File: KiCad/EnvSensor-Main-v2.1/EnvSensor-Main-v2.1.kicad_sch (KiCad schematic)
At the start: 90 parts, among them J6 POWER_INPUT, Q1 IRLML2502

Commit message: Finishing touhches on main board
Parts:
- D?: value SD_LED -> LED
- D?: value CPU_LED -> LED
- J?: footprint Connector_PinHeader_2.54mm:PinHeader_1x06_P2.54mm_Vertical -> Connector_JST:JST_PH_S6B-PH-SM4-TB_1x06-1MP_P2.00mm_Horizontal
- J?: footprint Connector_PinHeader_2.54mm:PinHeader_1x04_P2.54mm_Vertical -> Connector_JST:JST_PH_S4B-PH-SM4-TB_1x04-1MP_P2.00mm_Horizontal
- L?: footprint Inductor_SMD:L_0805_2012Metric -> Inductor_SMD:L_1206_3216Metric
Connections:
- net +5V: now also C23.1, C24.1, C25.1
- net BMP280_VCC: now also JP3.3 (B); no longer JP3.1 (A)
- net GND: now also C23.2, C24.2, C25.2, JP3.1 (A); no longer JP3.3 (B)
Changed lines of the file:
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@@
   (junction (at 346.71 190.5) (diameter 0) (color 0 0 0 0)
   )
+  (junction (at 386.08 39.37) (diameter 0) (color 0 0 0 0)
+  )
   (junction (at 232.41 194.31) (diameter 0) (color 0 0 0 0)
   )
   (junction (at 209.55 77.47) (diameter 0) (color 0 0 0 0)
   )
+  (junction (at 381 39.37) (diameter 0) (color 0 0 0 0)
+  )
   (junction (at 232.41 162.56) (diameter 0) (color 0 0 0 0)
   )
@@
   (junction (at 88.9 254) (diameter 0) (color 0 0 0 0)
   )
+  (junction (at 391.16 49.53) (diameter 0) (color 0 0 0 0)
+  )
+  (junction (at 386.08 49.53) (diameter 0) (color 0 0 0 0)
+  )
   (junction (at 101.6 29.21) (diameter 0) (color 0 0 0 0)
   )
@@
     (stroke (width 0) (type default))
   )
+  (wire (pts (xy 391.16 49.53) (xy 396.24 49.53))
+    (stroke (width 0) (type default))
+  )
   (wire (pts (xy 240.03 162.56) (xy 243.84 162.56))
     (stroke (width 0) (type default))
@@
     (stroke (width 0) (type default))
   )
+  (wire (pts (xy 377.19 39.37) (xy 381 39.37))
+    (stroke (width 0) (type default))
+  )
   (wire (pts (xy 34.29 113.03) (xy 26.67 113.03))
     (stroke (width 0) (type default))
@@
     (stroke (width 0) (type default))
   )
+  (wire (pts (xy 381 38.1) (xy 381 39.37))
+    (stroke (width 0) (type default))
+  )
   (polyline (pts (xy 148.59 283.21) (xy 148.59 223.52))
     (stroke (width 0) (type default))
@@
     (stroke (width 0) (type default))
   )
+  (wire (pts (xy 377.19 48.26) (xy 377.19 49.53))
+    (stroke (width 0) (type default))
+  )
   (polyline (pts (xy 231.14 96.52) (xy 231.14 22.86))
     (stroke (width 0) (type default))
@@
     (stroke (width 0) (type default))
   )
+  (wire (pts (xy 396.24 49.53) (xy 396.24 48.26))
+    (stroke (width 0) (type default))
+  )
   (wire (pts (xy 224.79 194.31) (xy 232.41 194.31))
     (stroke (width 0) (type default))
@@
     (stroke (width 0) (type default))
   )
+  (wire (pts (xy 377.19 49.53) (xy 386.08 49.53))
+    (stroke (width 0) (type default))
+  )
   (wire (pts (xy 48.26 252.73) (xy 48.26 254))
     (stroke (width 0) (type default))
@@
     (stroke (width 0) (type default))
   )
+  (wire (pts (xy 381 39.37) (xy 386.08 39.37))
+    (stroke (width 0) (type default))
+  )
   (wire (pts (xy 224.79 189.23) (xy 247.65 189.23))
     (stroke (width 0) (type default))
@@
     (stroke (width 0) (type default))
   )
+  (wire (pts (xy 386.08 39.37) (xy 386.08 40.64))
+    (stroke (width 0) (type default))
+  )
   (wire (pts (xy 92.71 29.21) (xy 92.71 31.75))
     (stroke (width 0) (type default))
@@
     (stroke (width 0) (type default))
   )
+  (wire (pts (xy 386.08 39.37) (xy 396.24 39.37))
+    (stroke (width 0) (type default))
+  )
   (wire (pts (xy 90.17 92.71) (xy 97.79 92.71))
     (stroke (width 0) (type default))
@@
     (stroke (width 0) (type default))
   )
+  (wire (pts (xy 396.24 39.37) (xy 396.24 40.64))
+    (stroke (width 0) (type default))
+  )
   (wire (pts (xy 248.92 256.54) (xy 246.38 256.54))
     (stroke (width 0) (type default))
@@
     (stroke (width 0) (type default))
   )
+  (wire (pts (xy 377.19 40.64) (xy 377.19 39.37))
+    (stroke (width 0) (type default))
+  )
   (wire (pts (xy 182.88 195.58) (xy 182.88 198.12))
     (stroke (width 0) (type default))
@@
     (stroke (width 0) (type default))
   )
+  (wire (pts (xy 386.08 49.53) (xy 391.16 49.53))
+    (stroke (width 0) (type default))
+  )
   (wire (pts (xy 86.36 255.27) (xy 86.36 254))
     (stroke (width 0) (type default))
@@
     (stroke (width 0) (type default))
   )
+  (wire (pts (xy 386.08 48.26) (xy 386.08 49.53))
+    (stroke (width 0) (type default))
+  )
   (wire (pts (xy 152.4 71.12) (xy 152.4 77.47))
     (stroke (width 0) (type default))
@@
     (stroke (width 0) (type default))
   )
+  (wire (pts (xy 391.16 49.53) (xy 391.16 52.07))
+    (stroke (width 0) (type default))
+  )
   (wire (pts (xy 44.45 176.53) (xy 53.34 176.53))
     (stroke (width 0) (type default))
@@
     )
   )
+  (symbol (lib_id "power:+5V") (at 381 38.1 0) (unit 1)
+    (in_bom yes) (on_board yes) (dnp no)
+    (property "Reference" "#PWR?" (at 381 41.91 0)
+      (effects (font (size 1.27 1.27)) hide)
+    )
+    (property "Value" "+5V" (at 381.381 33.7058 0)
+      (effects (font (size 1.27 1.27)))
+    )
+    (property "Footprint" "" (at 381 38.1 0)
+      (effects (font (size 1.27 1.27)) hide)
+    )
+    (property "Datasheet" "" (at 381 38.1 0)
+      (effects (font (size 1.27 1.27)) hide)
+    )
+    (pin "1")
+    (instances
+      (project "EnvSensor-v2"
+        (path "/03d24414-d9e0-4f5b-b242-97cf8b84dd63"
+          (reference "#PWR?") (unit 1)
+        )
+      )
+      (project "EnvSensor-Main-v2.1"
+        (path "/dfd093c6-2284-47ad-b656-d7ad8b97da97"
+          (reference "#PWR057") (unit 1)
+        )
+      )
+    )
+  )
   (symbol (lib_id "Device:R") (at 252.73 256.54 270) (unit 1)
     (in_bom yes) (on_board yes) (dnp no)
@@
       (effects (font (size 1.27 1.27)) (justify right))
     )
-    (property "Value" "SD_LED" (at 52.07 255.27 90)
+    (property "Value" "LED" (at 52.07 255.27 90)
       (effects (font (size 1.27 1.27)) (justify right))
     )
@@
       (effects (font (size 1.27 1.27)) (justify left))
     )
-    (property "Footprint" "Connector_PinHeader_2.54mm:PinHeader_1x06_P2.54mm_Vertical" (at 53.34 213.36 0)
+    (property "Footprint" "Connector_JST:JST_PH_S6B-PH-SM4-TB_1x06-1MP_P2.00mm_Horizontal" (at 53.34 213.36 0)
       (effects (font (size 1.27 1.27)) hide)
     )
@@
       (effects (font (size 1.27 1.27)) (justify left))
     )
-    (property "Footprint" "Connector_PinHeader_2.54mm:PinHeader_1x04_P2.54mm_Vertical" (at 377.19 57.15 0)
+    (property "Footprint" "Connector_JST:JST_PH_S4B-PH-SM4-TB_1x04-1MP_P2.00mm_Horizontal" (at 377.19 57.15 0)
       (effects (font (size 1.27 1.27)) hide)
     )
@@
       (effects (font (size 1.27 1.27)))
     )
-    (property "Footprint" "Inductor_SMD:L_0805_2012Metric" (at 83.82 29.21 0)
+    (property "Footprint" "Inductor_SMD:L_1206_3216Metric" (at 83.82 29.21 0)
       (effects (font (size 1.27 1.27)) hide)
     )
@@
     )
   )
+  (symbol (lib_id "power:GND") (at 391.16 52.07 0) (unit 1)
+    (in_bom yes) (on_board yes) (dnp no)
+    (property "Reference" "#PWR?" (at 391.16 58.42 0)
+      (effects (font (size 1.27 1.27)) hide)
+    )
+    (property "Value" "GND" (at 391.287 56.4642 0)
+      (effects (font (size 1.27 1.27)))
+    )
+    (property "Footprint" "" (at 391.16 52.07 0)
+      (effects (font (size 1.27 1.27)) hide)
+    )
+    (property "Datasheet" "" (at 391.16 52.07 0)
+      (effects (font (size 1.27 1.27)) hide)
+    )
+    (pin "1")
+    (instances
+      (project "EnvSensor-v2"
+        (path "/03d24414-d9e0-4f5b-b242-97cf8b84dd63"
+          (reference "#PWR?") (unit 1)
+        )
+      )
+      (project "EnvSensor-Main-v2.1"
+        (path "/dfd093c6-2284-47ad-b656-d7ad8b97da97"
+          (reference "#PWR056") (unit 1)
+        )
+      )
+    )
+  )
   (symbol (lib_id "EnvSensor-v2-rescue:Jumper_NO_Small-Device") (at 300.99 43.18 90) (unit 1)
     (in_bom yes) (on_board yes) (dnp no)
@@
       (effects (font (size 1.016 1.016)))
     )
-    (property "Value" "ESP-12S" (at 335.28 122.3772 0)
+    (property "Value" "ESP-12S" (at 339.09 125.73 0)
       (effects (font (size 1.016 1.016)))
     )
@@
       (effects (font (size 1.27 1.27)) (justify right))
     )
-    (property "Value" "CPU_LED" (at 31.75 255.27 90)
+    (property "Value" "LED" (at 31.75 255.27 90)
       (effects (font (size 1.27 1.27)) (justify right))
     )
@@
     )
   )
-  (symbol (lib_id "Jumper:Jumper_3_Bridged12") (at 293.37 57.15 270) (unit 1)
+  (symbol (lib_id "Jumper:Jumper_3_Bridged12") (at 293.37 57.15 270) (mirror x) (unit 1)
     (in_bom yes) (on_board yes) (dnp no)
-    (property "Reference" "JP3" (at 294.9962 56.5063 90)
+    (property "Reference" "JP3" (at 294.9962 57.7937 90)
       (effects (font (size 1.27 1.27)) (justify left))
     )
-    (property "Value" "Address" (at 294.64 58.42 90)
+    (property "Value" "Address" (at 294.64 55.88 90)
       (effects (font (size 1.27 1.27)) (justify left))
     )

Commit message: Finishing touches
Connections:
- net SCD_POWER: now reaches J?.1 (Pin_1), JP?.1, U?.1 (VDD), U?.19 (VDDH), U?.7 (VDD)

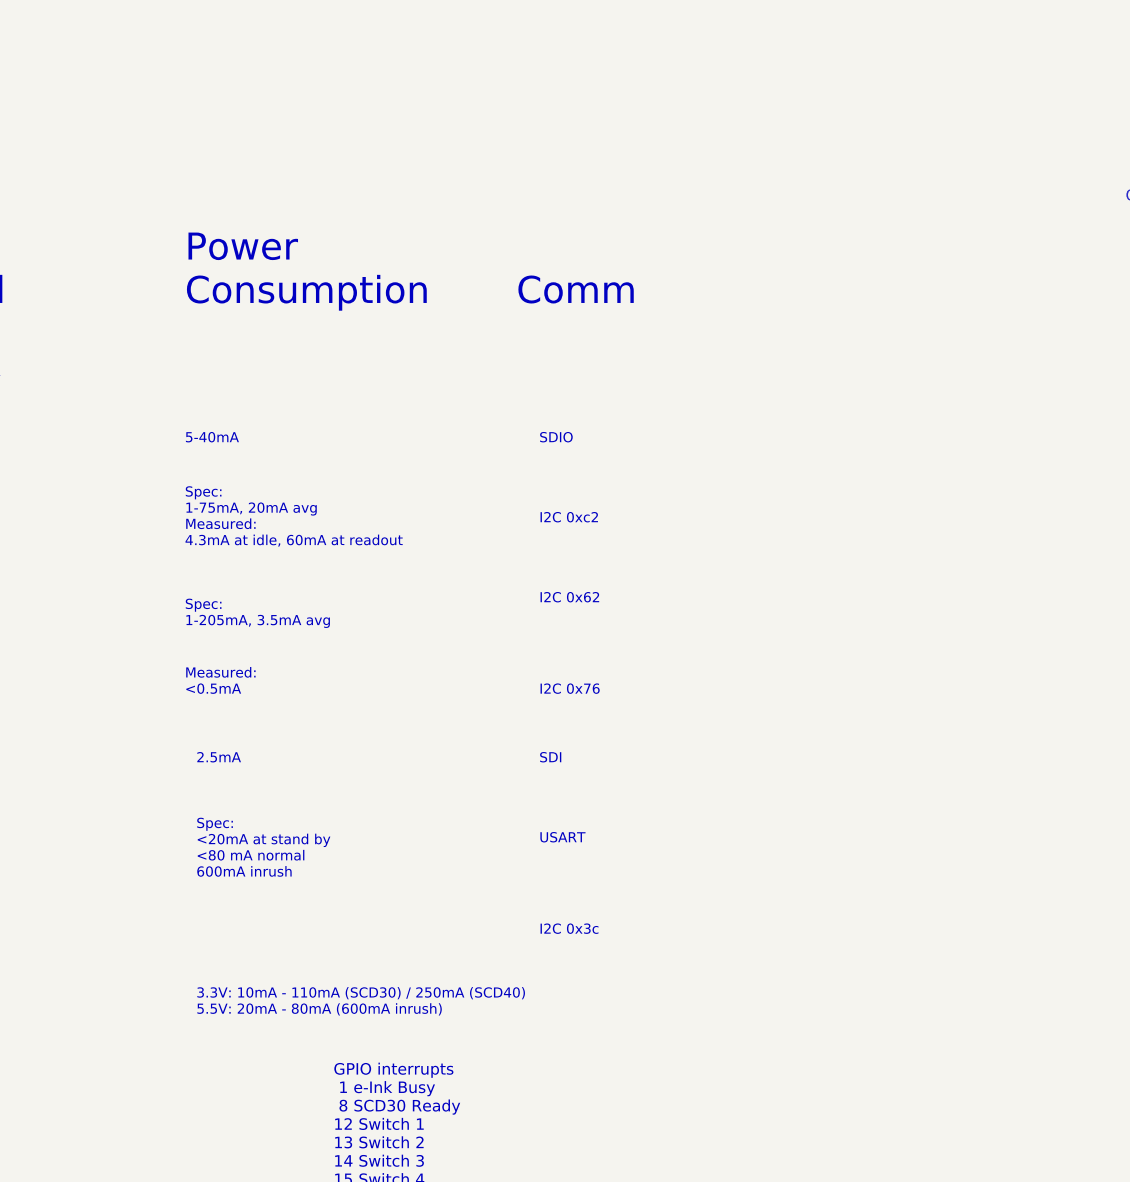
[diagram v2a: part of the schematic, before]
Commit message: LM2735 fixes
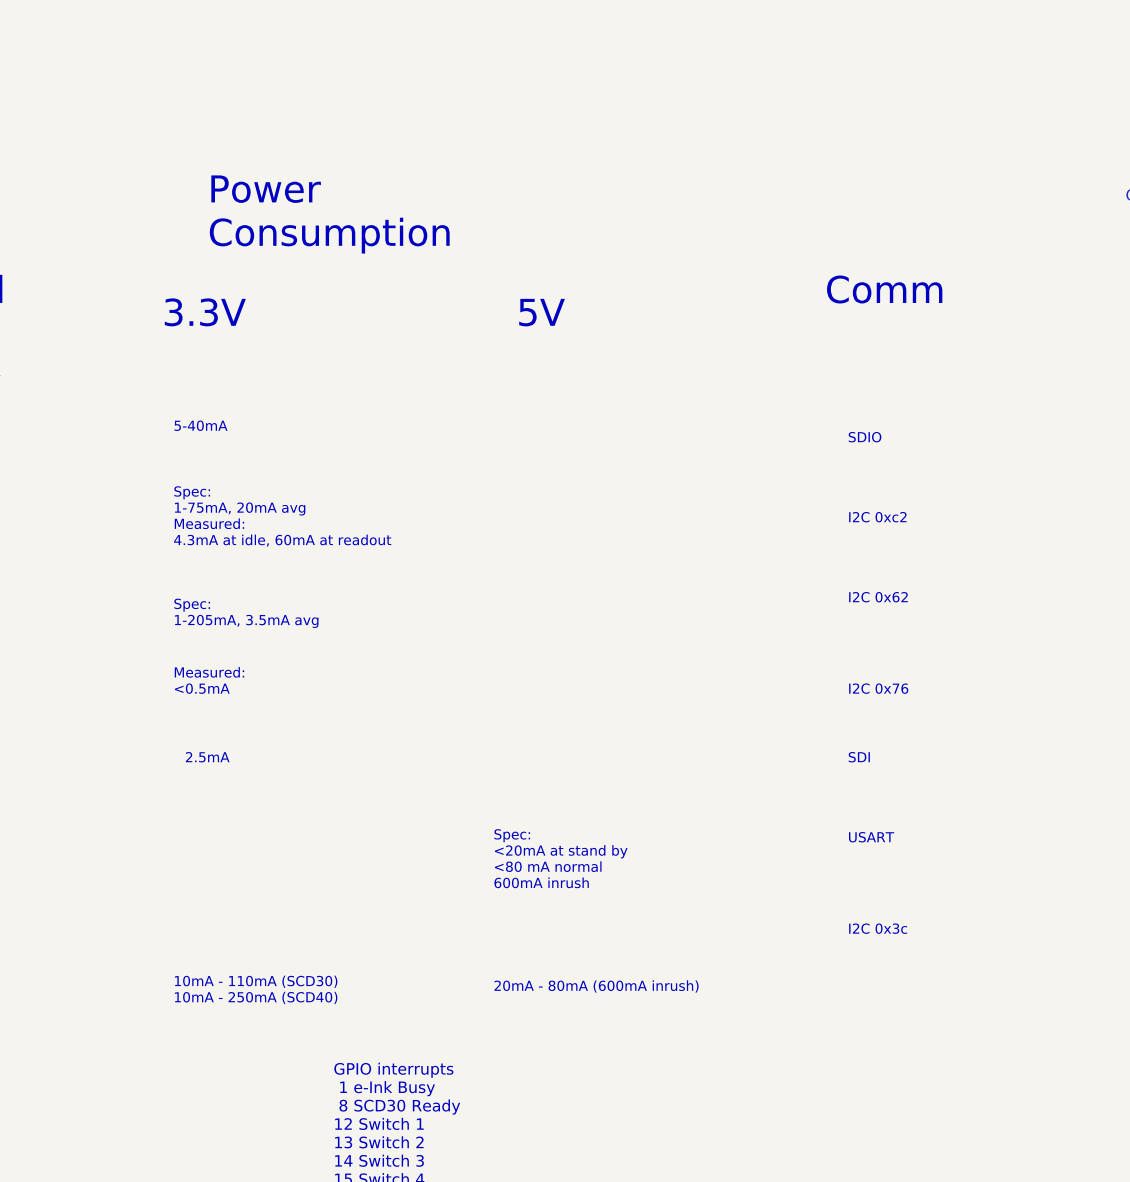
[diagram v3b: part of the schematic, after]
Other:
- note added: "10mA - 110mA (SCD30) 10mA - 250mA (SCD40)"
- note added: "20mA - 80mA (600mA inrush)"
- note added: "5V"
- note removed: "3.3V: 10mA - 110mA (SCD30) / 250mA (SCD40) 5.5V: 20mA - 80mA (600mA inrush)"
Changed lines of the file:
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@@
     (effects (font (size 2.9972 2.9972)) (justify right bottom))
   )
-  (text "Spec:\n1-205mA, 3.5mA avg\n" (at -86.36 161.29 0)
+  (text "Spec:\n1-205mA, 3.5mA avg\n" (at -87.63 161.29 0)
     (effects (font (size 1.1176 1.1176)) (justify left bottom))
   )
@@
     (effects (font (size 1.1176 1.1176)) (justify left bottom))
   )
-  (text "2.5mA" (at -85.09 176.53 0)
+  (text "2.5mA" (at -86.36 176.53 0)
     (effects (font (size 1.1176 1.1176)) (justify left bottom))
   )
-  (text "I2C 0xc2" (at -46.99 149.86 0)
+  (text "I2C 0xc2" (at -12.7 149.86 0)
     (effects (font (size 1.1176 1.1176)) (justify left bottom))
   )
-  (text "3.3V: 10mA - 110mA (SCD30) / 250mA (SCD40)\n5.5V: 20mA - 80mA (600mA inrush)"
-    (at -85.09 204.47 0)
+  (text "10mA - 110mA (SCD30)\n10mA - 250mA (SCD40)" (at -87.63 203.2 0)
     (effects (font (size 1.1176 1.1176)) (justify left bottom))
   )
-  (text "Comm" (at -49.53 125.73 0)
+  (text "Comm" (at -15.24 125.73 0)
     (effects (font (size 2.9972 2.9972)) (justify left bottom))
   )
@@
     (effects (font (size 1.1176 1.1176)) (justify left bottom))
   )
-  (text "5-40mA" (at -86.36 140.97 0)
+  (text "5-40mA" (at -87.63 139.7 0)
     (effects (font (size 1.1176 1.1176)) (justify left bottom))
   )
-  (text "I2C 0x3c" (at -46.99 195.58 0)
+  (text "I2C 0x3c" (at -12.7 195.58 0)
     (effects (font (size 1.1176 1.1176)) (justify left bottom))
   )
@@
   )
   (text "Input Switches" (at 196.85 233.68 0)
+    (effects (font (size 2.9972 2.9972)) (justify left bottom))
+  )
+  (text "3.3V" (at -88.9 128.27 0)
     (effects (font (size 2.9972 2.9972)) (justify left bottom))
   )
@@
     (effects (font (size 1.1176 1.1176)) (justify left bottom))
   )
-  (text "Measured:\n<0.5mA\n" (at -86.36 168.91 0)
+  (text "Measured:\n<0.5mA\n" (at -87.63 168.91 0)
     (effects (font (size 1.1176 1.1176)) (justify left bottom))
   )
-  (text "Power\nConsumption" (at -86.36 125.73 0)
+  (text "Power\nConsumption" (at -83.82 119.38 0)
     (effects (font (size 2.9972 2.9972)) (justify left bottom))
   )
@@
     (effects (font (size 2.9972 2.9972)) (justify left bottom))
   )
-  (text "I2C 0x62" (at -46.99 158.75 0)
+  (text "I2C 0x62" (at -12.7 158.75 0)
     (effects (font (size 1.1176 1.1176)) (justify left bottom))
   )
@@
     (effects (font (size 1.1176 1.1176)) (justify left bottom))
   )
-  (text "SDI" (at -46.99 176.53 0)
+  (text "SDI" (at -12.7 176.53 0)
     (effects (font (size 1.1176 1.1176)) (justify left bottom))
   )
@@
     (effects (font (size 1.1176 1.1176)) (justify left bottom))
   )
-  (text "I2C 0x76" (at -46.99 168.91 0)
+  (text "I2C 0x76" (at -12.7 168.91 0)
     (effects (font (size 1.1176 1.1176)) (justify left bottom))
   )
@@
     (effects (font (size 2.9972 2.9972)) (justify right bottom))
   )
+  (text "5V" (at -49.53 128.27 0)
+    (effects (font (size 2.9972 2.9972)) (justify left bottom))
+  )
   (text "NO analog input at PB6/58\nAvailable inputs: 14,15,20,22"
     (at -71.12 67.31 0)
@@
   )
   (text "Spec:\n1-75mA, 20mA avg\nMeasured:\n4.3mA at idle, 60mA at readout"
-    (at -86.36 152.4 0)
+    (at -87.63 152.4 0)
     (effects (font (size 1.1176 1.1176)) (justify left bottom))
   )
@@
     (effects (font (size 2.9972 2.9972)) (justify right bottom))
   )
-  (text "SDIO" (at -46.99 140.97 0)
+  (text "SDIO" (at -12.7 140.97 0)
     (effects (font (size 1.1176 1.1176)) (justify left bottom))
   )
   (text "Spec:\n<20mA at stand by\n<80 mA normal\n600mA inrush"
-    (at -85.09 189.23 0)
+    (at -52.07 190.5 0)
     (effects (font (size 1.1176 1.1176)) (justify left bottom))
   )
@@
     (effects (font (size 1.27 1.27)) (justify left bottom))
   )
-  (text "USART" (at -46.99 185.42 0)
+  (text "USART" (at -12.7 185.42 0)
     (effects (font (size 1.1176 1.1176)) (justify left bottom))
   )
+  (text "20mA - 80mA (600mA inrush)" (at -52.07 201.93 0)
+    (effects (font (size 1.1176 1.1176)) (justify left bottom))
+  )

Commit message: More fixes
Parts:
- C25: footprint Capacitor_SMD:CP_Elec_6.3x5.8 -> Capacitor_SMD:CP_Elec_4x5.3
- J?: footprint Connector_PinSocket_2.54mm:PinSocket_1x04_P2.54mm_Vertical -> Connector_PinSocket_2.54mm:PinSocket_1x04_P2.54mm_Horizontal
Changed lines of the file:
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@@
       (effects (font (size 1.27 1.27)) (justify left))
     )
-    (property "Footprint" "Capacitor_SMD:CP_Elec_6.3x5.8" (at 378.1552 48.26 0)
+    (property "Footprint" "Capacitor_SMD:CP_Elec_4x5.3" (at 378.1552 48.26 0)
       (effects (font (size 1.27 1.27)) hide)
     )
@@
       (effects (font (size 1.27 1.27)) (justify left))
     )
-    (property "Footprint" "Connector_PinSocket_2.54mm:PinSocket_1x04_P2.54mm_Vertical" (at 96.52 219.71 0)
-      (effects (font (size 1.27 1.27)) hide)
-    )
+    (property "Footprint" "Connector_PinSocket_2.54mm:PinSocket_1x04_P2.54mm_Horizontal" (at 96.52 219.71 0)
+      (effects (font (size 1.27 1.27)) hide)
+    )

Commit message: More fixes
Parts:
- added H5, H6: MountingHole, TestPoint:TestPoint_THTPad_D1.5mm_Drill0.7mm, symbol Mechanical:MountingHole
- L?: footprint Inductor_SMD:L_1206_3216Metric -> Inductor_SMD:L_1210_3225Metric
- Q1: footprint Package_TO_SOT_SMD:SOT-23 -> Package_TO_SOT_SMD:SOT-23-3
- Q?: footprint Package_TO_SOT_SMD:TSOT-23-6 -> Package_TO_SOT_SMD:TSOT-23-6_HandSoldering
- SW?: footprint Button_Switch_THT:SW_Tactile_SKHH_Angled -> Button_Switch_THT:SW_Tactile_SPST_Angled_PTS645Vx83-2LFS
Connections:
- net GND: now also D?.1 (K), D?.1 (K), D?.1 (K), D?.1 (K), D?.1 (K), D?.1 (K), D?.1 (K), D?.1 (K); no longer R?.2, R?.2, R?.2, R?.2
- net LED_1: now also R?.1; no longer D?.2 (A), D?.2 (A)
- net LED_2: now also R?.1; no longer D?.2 (A), D?.2 (A)
- net LED_3: now also R?.1; no longer D?.2 (A), D?.2 (A)
- net LED_4: now also R?.1; no longer D?.2 (A), D?.2 (A)
- new net: D?.2 (A), D?.2 (A), R?.2 (x4)
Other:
- moved on the sheet: D?, R?

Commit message: More work
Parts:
- J? (x3): footprint Connector_PinHeader_2.54mm:PinHeader_1x02_P2.54mm_Vertical -> Connector_PinHeader_2.54mm:PinHeader_1x02_P2.54mm_Horizontal
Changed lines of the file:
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@@
       (effects (font (size 1.27 1.27)) (justify left))
     )
-    (property "Footprint" "Connector_PinHeader_2.54mm:PinHeader_1x02_P2.54mm_Vertical" (at 294.64 44.45 0)
+    (property "Footprint" "Connector_PinHeader_2.54mm:PinHeader_1x02_P2.54mm_Horizontal" (at 294.64 44.45 0)
       (effects (font (size 1.27 1.27)) hide)
     )
@@
       (effects (font (size 1.27 1.27)) (justify left))
     )
-    (property "Footprint" "Connector_PinHeader_2.54mm:PinHeader_1x02_P2.54mm_Vertical" (at 251.46 127 0)
+    (property "Footprint" "Connector_PinHeader_2.54mm:PinHeader_1x02_P2.54mm_Horizontal" (at 251.46 127 0)
       (effects (font (size 1.27 1.27)) hide)
     )
@@
       (effects (font (size 1.27 1.27)) (justify left))
     )
-    (property "Footprint" "Connector_PinHeader_2.54mm:PinHeader_1x02_P2.54mm_Vertical" (at 181.61 50.8 0)
+    (property "Footprint" "Connector_PinHeader_2.54mm:PinHeader_1x02_P2.54mm_Horizontal" (at 181.61 50.8 0)
       (effects (font (size 1.27 1.27)) hide)
     )
